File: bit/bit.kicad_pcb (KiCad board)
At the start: 2 copper layers, 15 x 20 mm, 12 parts, among them J1 MID, J10 COL, J11 ROW, J2 COL, J3 ROW, J4 COL, J5 ROW, J6 COL, J7 ROW, J8 COL, J9 ROW

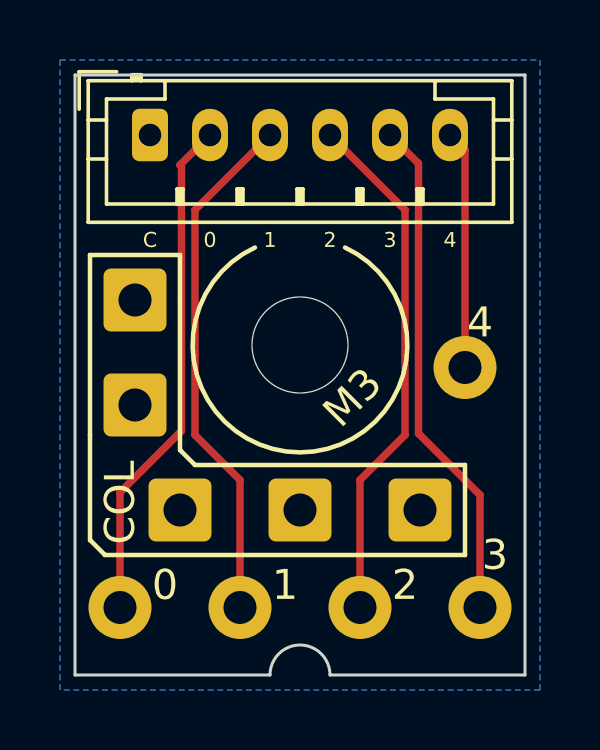
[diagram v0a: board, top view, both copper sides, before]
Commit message: Use SMD pads for the Bit
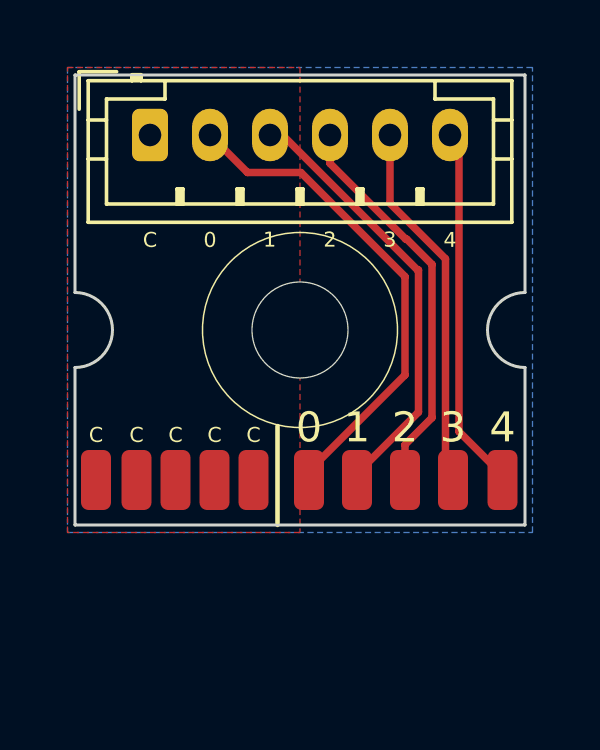
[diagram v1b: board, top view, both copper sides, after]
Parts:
- J10, J11, J2, J3, J4, J5, J6, J7, J8, J9: footprint Connector_Wire:SolderWire-0.5sqmm_1x01_D0.9mm_OD2.1mm -> Connector_Wire:SolderWirePad_1x01_SMD_1x2mm
- moved J6 8.21 mm to (144.3, 80.0)
- moved J3 7.60 mm to (148.8, 80.0)
- moved J10 7.18 mm to (146.9, 80.0)
- moved J9 5.77 mm to (150.4, 80.0)
- moved J11 4.51 mm to (152.0, 80.0)
- moved J5 4.34 mm to (153.6, 80.0)
- moved J7 3.95 mm to (155.2, 80.0)
- moved J8 3.02 mm to (145.7, 80.0)
- moved J2 2.97 mm to (141.7, 80.0)
- moved J4 2.50 mm to (143.1, 80.0)
- moved H1 0.50 mm to (148.5, 75.0)
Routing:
- net /ROW3: track 17.0 -> 12.4 mm
- net /ROW4: track 7.96 -> 12.2 mm
- net /ROW2: track 17.4 -> 13.3 mm
- net /ROW1: track 17.4 -> 14.7 mm
- added copper zone on F.Cu, net /COL
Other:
- board size 15 x 20 mm -> 15 x 15 mm
- board text added: "github.com/encukou/squeezebar"
- board text removed: "COL"
